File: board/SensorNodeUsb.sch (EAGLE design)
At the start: 15 parts, among them J1 JP5E, X2 USBPCB

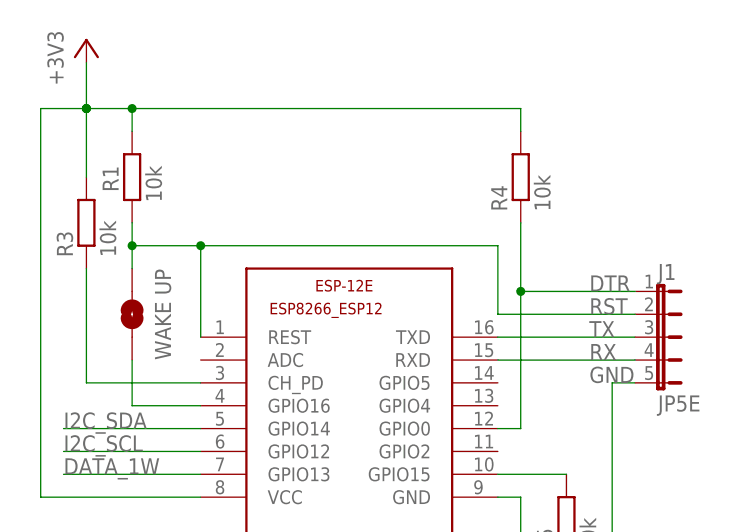
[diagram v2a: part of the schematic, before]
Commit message: change programming interface
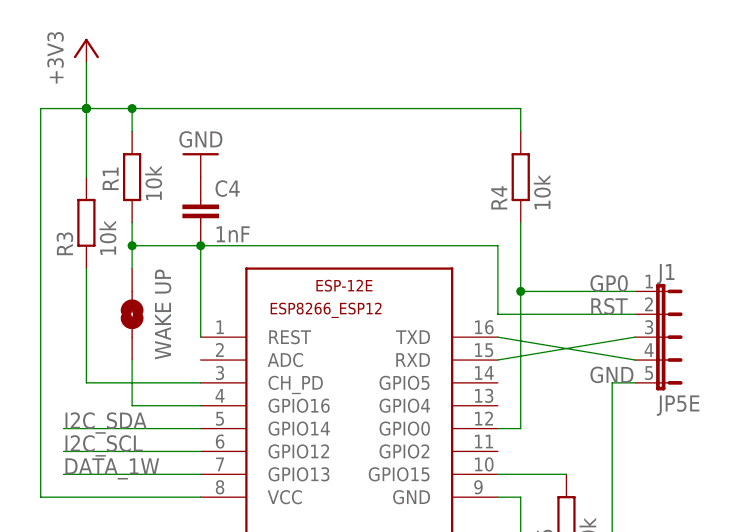
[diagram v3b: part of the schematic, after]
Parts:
- added C4: 1nF, rcl:C-EUC1206
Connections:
- net DTR renamed GP0
- removed net RX: ESP-12E.RXD, J1.4
- removed net TX: ESP-12E.TXD, J1.3
- new net N$1: ESP-12E.RXD, J1.3
- new net N$4: ESP-12E.TXD, J1.4
- net GND: now also C4.1
- net RST: now also C4.2
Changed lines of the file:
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@@
 </classes>
 <parts>
-<part name="FRAME1" library="frames" library_urn="urn:adsk.eagle:library:229" deviceset="DINA4_L" device=""/>
 <part name="ESP-12E" library="ESP8266-ESP12E" deviceset="ESP8266-12" device=""/>
 <part name="C1" library="rcl" library_urn="urn:adsk.eagle:library:334" deviceset="C-EU" device="C1206" package3d_urn="urn:adsk.eagle:package:23618/2" value="2uF"/>
@@
 <part name="J1" library="thomo" deviceset="JP5E" device="" package3d_urn="urn:adsk.eagle:package:11605224/1"/>
 <part name="R5" library="rcl" library_urn="urn:adsk.eagle:library:334" deviceset="R-EU_" device="M1206" package3d_urn="urn:adsk.eagle:package:23566/2" value="10k"/>
+<part name="FRAME2" library="SparkFun-Aesthetics" library_urn="urn:adsk.eagle:library:507" deviceset="FRAME-A4L" device="">
+<attribute name="CNAME" value="https://github.com/thomo/sensornode"/>
+<attribute name="CREVISION" value="v2.0"/>
+<attribute name="DESIGNER" value="ThoMo"/>
+</part>
+<part name="C4" library="rcl" library_urn="urn:adsk.eagle:library:334" deviceset="C-EU" device="C1206" package3d_urn="urn:adsk.eagle:package:23618/2" value="1nF"/>
+<part name="GND3" library="supply1" library_urn="urn:adsk.eagle:library:371" deviceset="GND" device=""/>
 </parts>
 <sheets>
@@
 </plain>
 <instances>
-<instance part="FRAME1" gate="G$1" x="0" y="0" smashed="yes"/>
-<instance part="FRAME1" gate="G$2" x="162.56" y="0" smashed="yes">
-<attribute name="LAST_DATE_TIME" x="175.26" y="1.27" size="2.54" layer="94"/>
-<attribute name="SHEET" x="248.92" y="1.27" size="2.54" layer="94"/>
-<attribute name="DRAWING_NAME" x="180.34" y="19.05" size="2.54" layer="94"/>
-</instance>
 <instance part="ESP-12E" gate="G$1" x="170.18" y="116.84" smashed="yes">
 <attribute name="NAME" x="160.02" y="129.54" size="1.27" layer="94"/>
@@
 <attribute name="NAME" x="186.4614" y="100.33" size="1.778" layer="95" rot="R90"/>
 <attribute name="VALUE" x="191.262" y="100.33" size="1.778" layer="96" rot="R90"/>
+</instance>
+<instance part="FRAME2" gate="G$1" x="3.81" y="3.81" smashed="yes">
+<attribute name="DRAWING_NAME" x="185.42" y="15.24" size="2.54" layer="94" font="vector"/>
+<attribute name="LAST_DATE_TIME" x="185.42" y="10.16" size="2.286" layer="94" font="vector"/>
+<attribute name="SHEET" x="199.39" y="5.08" size="2.54" layer="94" font="vector"/>
+<attribute name="CNAME" x="185.42" y="20.32" size="2.54" layer="94" font="vector"/>
+<attribute name="CREVISION" x="238.73" y="4.98" size="2.54" layer="94" font="vector"/>
+<attribute name="DESIGNER" x="230.07" y="10.16" size="2.54" layer="94" font="vector"/>
+</instance>
+<instance part="C4" gate="G$1" x="147.32" y="139.7" smashed="yes">
+<attribute name="NAME" x="148.844" y="140.081" size="1.778" layer="95"/>
+<attribute name="VALUE" x="148.844" y="135.001" size="1.778" layer="96"/>
+</instance>
+<instance part="GND3" gate="1" x="147.32" y="144.78" smashed="yes" rot="R180">
+<attribute name="VALUE" x="149.86" y="147.32" size="1.778" layer="96" rot="R180"/>
 </instance>
 </instances>
@@
 <pinref part="GND7" gate="1" pin="GND"/>
 <wire x1="106.68" y1="132.08" x2="106.68" y2="127" width="0.1524" layer="91"/>
+</segment>
+<segment>
+<pinref part="C4" gate="G$1" pin="1"/>
+<pinref part="GND3" gate="1" pin="GND"/>
 </segment>
 </net>
@@
 <wire x1="180.34" y1="127" x2="195.58" y2="127" width="0.1524" layer="91"/>
 <label x="190.5" y="127" size="1.778" layer="95"/>
+<pinref part="C4" gate="G$1" pin="2"/>
 </segment>
 </net>
@@
 </segment>
 </net>
-<net name="DTR" class="0">
+<net name="GP0" class="0">
 <segment>
 <pinref part="R4" gate="G$1" pin="1"/>
@@
 </segment>
 </net>
-<net name="TX" class="0">
-<segment>
-<pinref part="ESP-12E" gate="G$1" pin="TXD"/>
-<wire x1="180.34" y1="124.46" x2="195.58" y2="124.46" width="0.1524" layer="91"/>
-<pinref part="J1" gate="G$1" pin="3"/>
-<label x="190.5" y="124.46" size="1.778" layer="95"/>
-</segment>
-</net>
-<net name="RX" class="0">
-<segment>
-<pinref part="ESP-12E" gate="G$1" pin="RXD"/>
-<wire x1="180.34" y1="121.92" x2="195.58" y2="121.92" width="0.1524" layer="91"/>
-<pinref part="J1" gate="G$1" pin="4"/>
-<label x="190.5" y="121.92" size="1.778" layer="95"/>
-</segment>
-</net>
 <net name="N$8" class="0">
 <segment>
@@
 </segment>
 </net>
+<net name="N$1" class="0">
+<segment>
+<pinref part="ESP-12E" gate="G$1" pin="RXD"/>
+<pinref part="J1" gate="G$1" pin="3"/>
+<wire x1="180.34" y1="121.92" x2="195.58" y2="124.46" width="0.1524" layer="91"/>
+</segment>
+</net>
+<net name="N$4" class="0">
+<segment>
+<pinref part="ESP-12E" gate="G$1" pin="TXD"/>
+<pinref part="J1" gate="G$1" pin="4"/>
+<wire x1="180.34" y1="124.46" x2="195.58" y2="121.92" width="0.1524" layer="91"/>
+</segment>
+</net>
